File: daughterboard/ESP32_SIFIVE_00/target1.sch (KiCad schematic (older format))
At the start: 0 parts

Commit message: further work on ESP32/SIFIVE daughterboard
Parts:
- added C? (x2): 1u, symbol Device:C_Small
- added C? (x9): 100n, symbol Device:C_Small
- added C?: 10u, symbol Device:C_Small
- added IC?: W25X40CLSNIG, hive_daughterboard:W25X40CLSNIG, symbol hive_daughterboard:W25X40CLSNIG
- added JP?: NRST, symbol Jumper:SolderJumper_2_Open
- added JP?: BOOT, symbol Jumper:SolderJumper_2_Open
- added R? (x3): 10k, symbol Device:R_Small
- added R? (x4): 100k, symbol Device:R_Small
- added U?: ESP32-S2, hive_daughterboard:ESP32-S2, symbol hive_daughterboard:ESP32-S2
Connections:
- net +3V3: now also C?.1, C?.1, C?.1, C?.1, C?.1, C?.1, C?.1, C?.1, C?.1, R?.1, R?.2, R?.2, U?.1 (VDDA@0), U?.20 (VDD3P3_RTC), U?.27 (VDD3P3_RTC_IO), U?.3 (VDD3P3@0), U?.4 (VDD3P3@1), U?.45 (VDD3P3_CPU), U?.51 (VDDA@1), U?.54 (VDDA@2)
- net GPIO1.0: now also U?.15 (IO10)
- net GPIO1.1: now also U?.16 (IO11)
- net GPIO1.2: now also U?.17 (IO12)
- net GPIO1.3: now also U?.18 (IO13)
- net RST_1: now also C?.1, JP?.1 (A), R?.1, U?.56 (CHIP_PU)
- net TCK|SWDCLK_1: now also R?.1, U?.43 (MTCK)
- net TDI|NC_1: now also U?.46 (MTDI)
- net TDO|SWO_1: now also U?.44 (MTD0)
- net TMS|SWDIO_1: now also R?.1, U?.47 (MTMS)
- net UART_RxD1: now also U?.48 (U0TXD)
- net UART_TxD1: now also U?.49 (U0RXD)
- new net: R?.2, U?.50 (IO45)
- new net: R?.2, U?.55 (IO46)
- new net BOOT: JP?.2 (B), R?.2, U?.5 (IO0)
- new net CLK: IC?.6 (CLK), U?.34 (SPICLK)
- new net CS: IC?.1 (/CS), R?.1, U?.33 (SPICS0)
- new net DI: IC?.5 (DI(IO0)), U?.36 (SPID)
- new net DO: IC?.2 (DO(IO1)), U?.35 (SPIQ)
- new net GND: C?.2, C?.2, C?.2, C?.2, C?.2, C?.2, C?.2, C?.2, C?.2, C?.2, C?.2, C?.2, IC?.4 (GND), JP?.1 (A), JP?.2 (B), R?.1, R?.1, R?.2, U?.57 (GND@0)
- new net HOLD: IC?.7 (/HOLD), U?.31 (SPIHD)
- new net VDD_SPI: C?.1, C?.1, IC?.8 (VCC), R?.2, U?.30 (VDD_SPI)
- new net WP: IC?.3 (/WP), U?.32 (SPIWP)
- no-connect marks 0 -> 27
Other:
- note added: "External Flash 512kB"
- note removed: "Power"

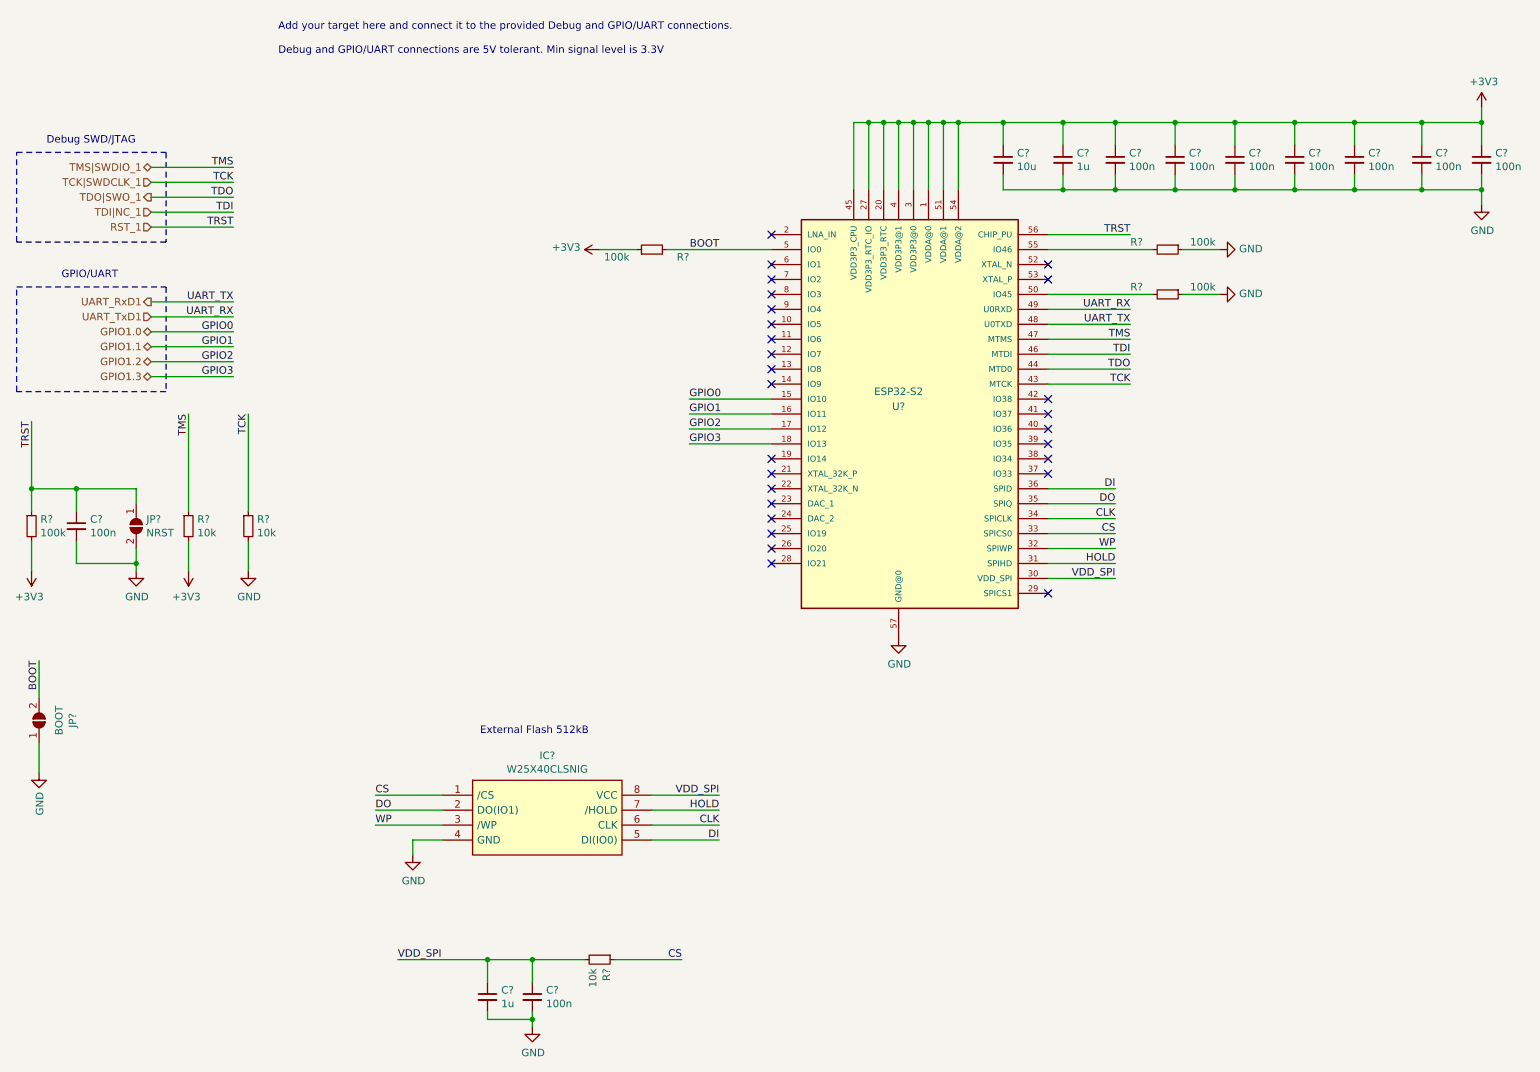
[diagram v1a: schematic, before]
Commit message: ERC on daughterboards
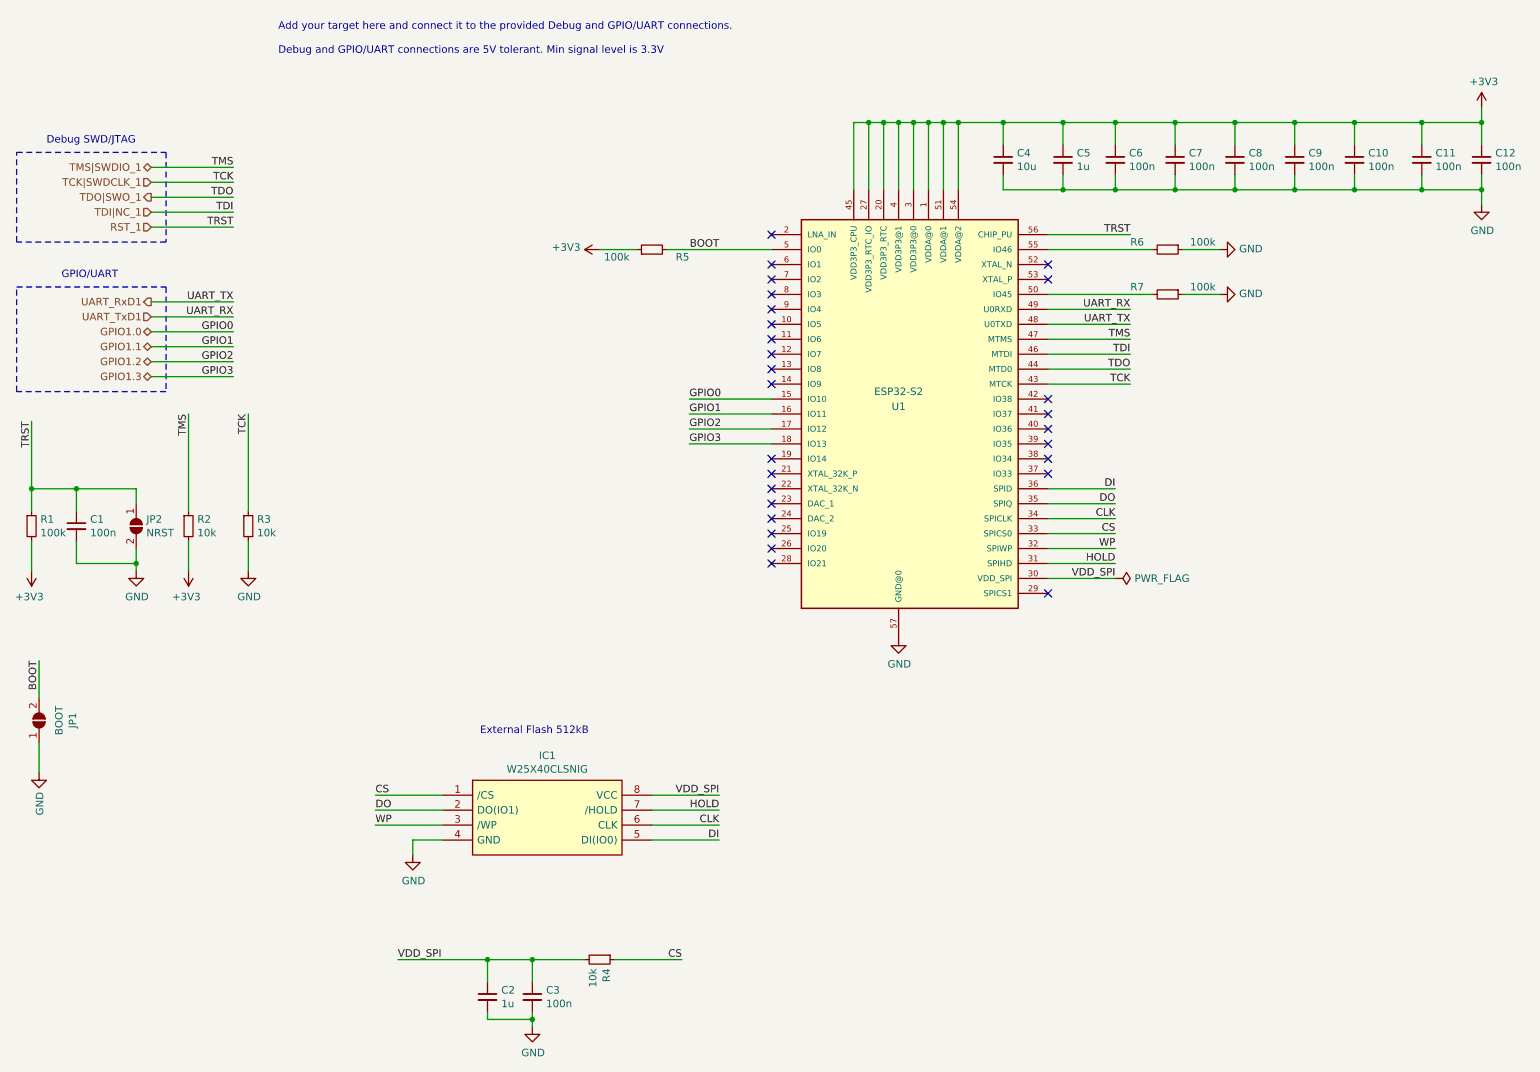
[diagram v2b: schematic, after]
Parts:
- gave numbers to parts that had none: 23

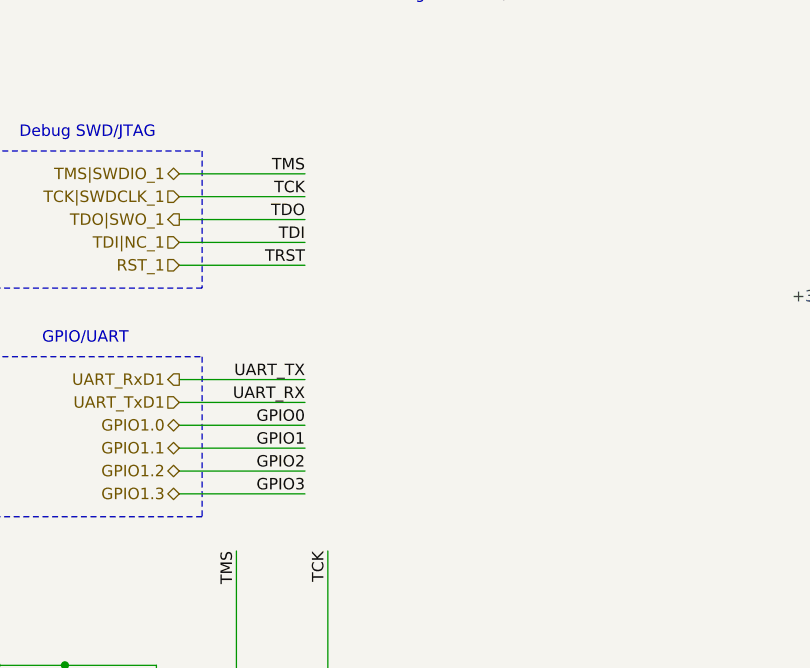
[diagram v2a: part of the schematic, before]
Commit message: added testpoints to daughterboards, updated readme
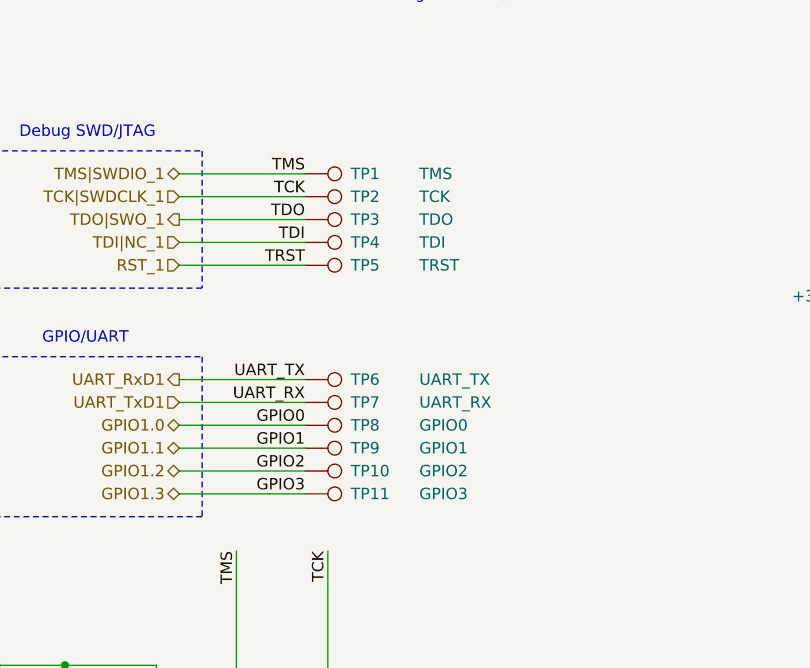
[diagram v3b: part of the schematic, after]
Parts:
- added TP1: TMS, symbol Connector:TestPoint
- added TP10: GPIO2, symbol Connector:TestPoint
- added TP11: GPIO3, symbol Connector:TestPoint
- added TP2: TCK, symbol Connector:TestPoint
- added TP3: TDO, symbol Connector:TestPoint
- added TP4: TDI, symbol Connector:TestPoint
- added TP5: TRST, symbol Connector:TestPoint
- added TP6: UART_TX, symbol Connector:TestPoint
- added TP7: UART_RX, symbol Connector:TestPoint
- added TP8: GPIO0, symbol Connector:TestPoint
- added TP9: GPIO1, symbol Connector:TestPoint
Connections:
- net GPIO1.0: now also TP8.1
- net GPIO1.1: now also TP9.1
- net GPIO1.2: now also TP10.1
- net GPIO1.3: now also TP11.1
- net RST_1: now also TP5.1
- net TCK|SWDCLK_1: now also TP2.1
- net TDI|NC_1: now also TP4.1
- net TDO|SWO_1: now also TP3.1
- net TMS|SWDIO_1: now also TP1.1
- net UART_RxD1: now also TP6.1
- net UART_TxD1: now also TP7.1
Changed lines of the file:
@@
+	0    1    1    0
+$EndComp
+$Comp
+L Connector:TestPoint TP?
+U 1 1 61926804
+P 2150 1700
+AR Path="/616688D6/61926804" Ref="TP?"  Part="1"
+AR Path="/61667F91/61926804" Ref="TP1"  Part="1"
+F 0 "TP1" V 2150 1900 50  0000 L CNN
+F 1 "TMS" V 2150 2200 50  0000 L CNN
+F 2 "" H 2350 1700 50  0001 C CNN
+F 3 "~" H 2350 1700 50  0001 C CNN
+	1    2150 1700
+	0    1    1    0
+$EndComp
+$Comp
+L Connector:TestPoint TP?
+U 1 1 6192680A
+P 2150 1800
+AR Path="/616688D6/6192680A" Ref="TP?"  Part="1"
+AR Path="/61667F91/6192680A" Ref="TP2"  Part="1"
+F 0 "TP2" V 2150 2000 50  0000 L CNN
+F 1 "TCK" V 2150 2300 50  0000 L CNN
+F 2 "" H 2350 1800 50  0001 C CNN
+F 3 "~" H 2350 1800 50  0001 C CNN
+	1    2150 1800
+	0    1    1    0
+$EndComp
+$Comp
+L Connector:TestPoint TP?
+U 1 1 61926810
+P 2150 1900
+AR Path="/616688D6/61926810" Ref="TP?"  Part="1"
+AR Path="/61667F91/61926810" Ref="TP3"  Part="1"
+F 0 "TP3" V 2150 2100 50  0000 L CNN
+F 1 "TDO" V 2150 2400 50  0000 L CNN
+F 2 "" H 2350 1900 50  0001 C CNN
+F 3 "~" H 2350 1900 50  0001 C CNN
+	1    2150 1900
+	0    1    1    0
+$EndComp
+$Comp
+L Connector:TestPoint TP?
+U 1 1 61926816
+P 2150 2000
+AR Path="/616688D6/61926816" Ref="TP?"  Part="1"
+AR Path="/61667F91/61926816" Ref="TP4"  Part="1"
+F 0 "TP4" V 2150 2200 50  0000 L CNN
+F 1 "TDI" V 2150 2500 50  0000 L CNN
+F 2 "" H 2350 2000 50  0001 C CNN
+F 3 "~" H 2350 2000 50  0001 C CNN
+	1    2150 2000
+	0    1    1    0
+$EndComp
+$Comp
+L Connector:TestPoint TP?
+U 1 1 6192681C
+P 2150 2100
+AR Path="/616688D6/6192681C" Ref="TP?"  Part="1"
+AR Path="/61667F91/6192681C" Ref="TP5"  Part="1"
+F 0 "TP5" V 2150 2300 50  0000 L CNN
+F 1 "TRST" V 2150 2600 50  0000 L CNN
+F 2 "" H 2350 2100 50  0001 C CNN
+F 3 "~" H 2350 2100 50  0001 C CNN
+	1    2150 2100
+	0    1    1    0
+$EndComp
+$Comp
+L Connector:TestPoint TP?
+U 1 1 61926822
+P 2150 2600
+AR Path="/616688D6/61926822" Ref="TP?"  Part="1"
+AR Path="/61667F91/61926822" Ref="TP6"  Part="1"
+F 0 "TP6" V 2150 2800 50  0000 L CNN
+F 1 "UART_TX" V 2150 3100 50  0000 L CNN
+F 2 "" H 2350 2600 50  0001 C CNN
+F 3 "~" H 2350 2600 50  0001 C CNN
+	1    2150 2600
+	0    1    1    0
+$EndComp
+$Comp
+L Connector:TestPoint TP?
+U 1 1 61926828
+P 2150 2700
+AR Path="/616688D6/61926828" Ref="TP?"  Part="1"
+AR Path="/61667F91/61926828" Ref="TP7"  Part="1"
+F 0 "TP7" V 2150 2900 50  0000 L CNN
+F 1 "UART_RX" V 2150 3200 50  0000 L CNN
+F 2 "" H 2350 2700 50  0001 C CNN
+F 3 "~" H 2350 2700 50  0001 C CNN
+	1    2150 2700
+	0    1    1    0
+$EndComp
+$Comp
+L Connector:TestPoint TP?
+U 1 1 6192682E
+P 2150 2800
+AR Path="/616688D6/6192682E" Ref="TP?"  Part="1"
+AR Path="/61667F91/6192682E" Ref="TP8"  Part="1"
+F 0 "TP8" V 2150 3000 50  0000 L CNN
+F 1 "GPIO0" V 2150 3300 50  0000 L CNN
+F 2 "" H 2350 2800 50  0001 C CNN
+F 3 "~" H 2350 2800 50  0001 C CNN
+	1    2150 2800
+	0    1    1    0
+$EndComp
+$Comp
+L Connector:TestPoint TP?
+U 1 1 61926834
+P 2150 2900
+AR Path="/616688D6/61926834" Ref="TP?"  Part="1"
+AR Path="/61667F91/61926834" Ref="TP9"  Part="1"
+F 0 "TP9" V 2150 3100 50  0000 L CNN
+F 1 "GPIO1" V 2150 3400 50  0000 L CNN
+F 2 "" H 2350 2900 50  0001 C CNN
+F 3 "~" H 2350 2900 50  0001 C CNN
+	1    2150 2900
+	0    1    1    0
+$EndComp
+$Comp
+L Connector:TestPoint TP?
+U 1 1 6192683A
+P 2150 3000
+AR Path="/616688D6/6192683A" Ref="TP?"  Part="1"
+AR Path="/61667F91/6192683A" Ref="TP10"  Part="1"
+F 0 "TP10" V 2150 3200 50  0000 L CNN
+F 1 "GPIO2" V 2150 3500 50  0000 L CNN
+F 2 "" H 2350 3000 50  0001 C CNN
+F 3 "~" H 2350 3000 50  0001 C CNN
+	1    2150 3000
+	0    1    1    0
+$EndComp
+$Comp
+L Connector:TestPoint TP?
+U 1 1 61926840
+P 2150 3100
+AR Path="/616688D6/61926840" Ref="TP?"  Part="1"
+AR Path="/61667F91/61926840" Ref="TP11"  Part="1"
+F 0 "TP11" V 2150 3300 50  0000 L CNN
+F 1 "GPIO3" V 2150 3600 50  0000 L CNN
+F 2 "" H 2350 3100 50  0001 C CNN
+F 3 "~" H 2350 3100 50  0001 C CNN
+	1    2150 3100
 	0    1    1    0
 $EndComp
